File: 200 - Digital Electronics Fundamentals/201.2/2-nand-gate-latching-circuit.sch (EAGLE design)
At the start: 5 parts, among them IC1 74ALS00N

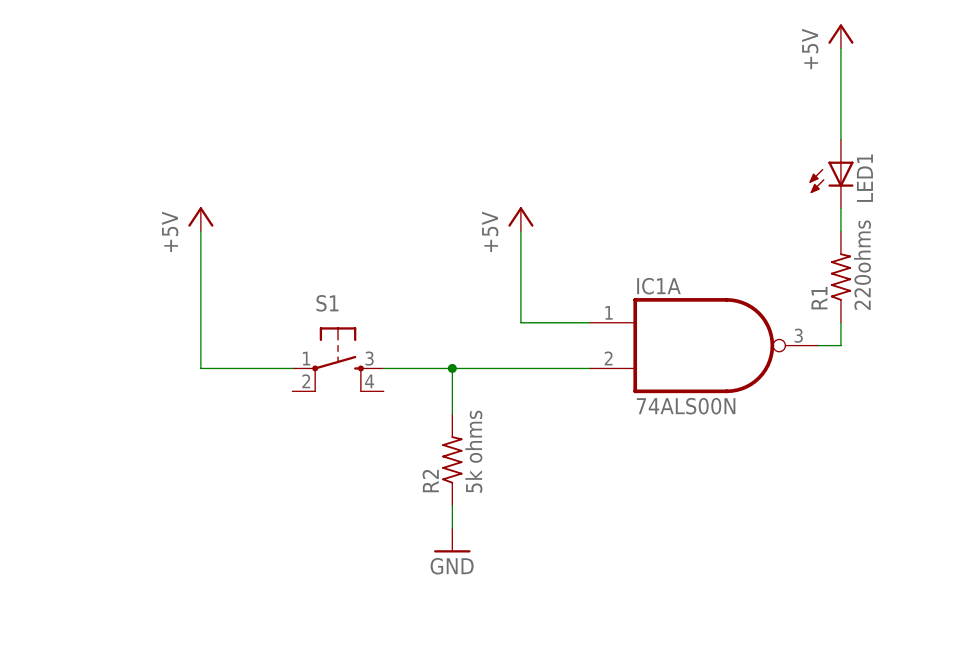
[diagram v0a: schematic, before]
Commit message: Made minor changes to Lab2 schematic.
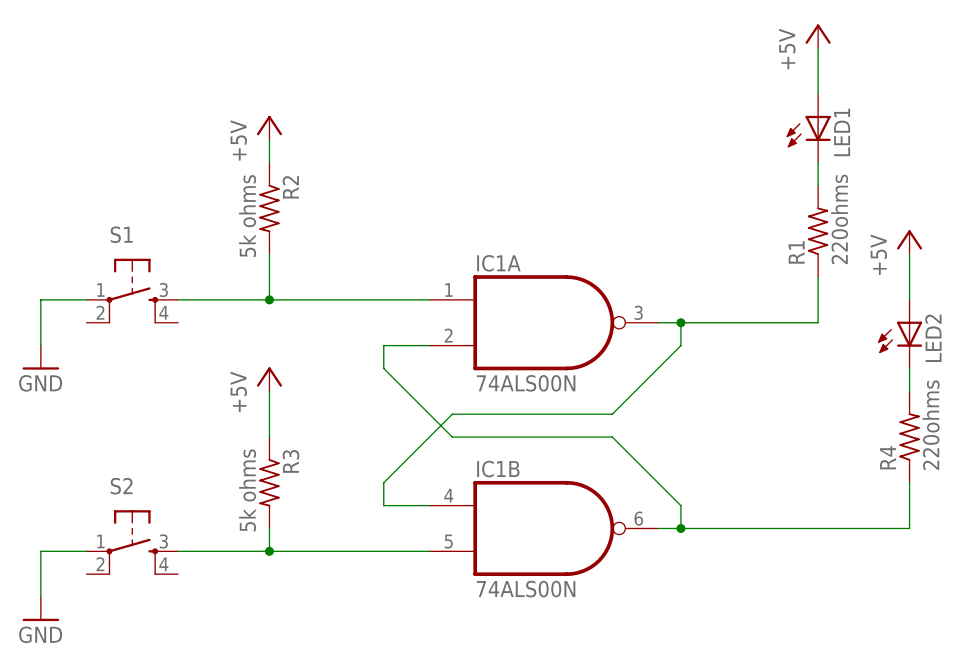
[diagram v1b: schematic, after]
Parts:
- added LED2: (no value), adafruit:LED5MM
- added R3: 5k ohms, resistor:R-US_0204/7
- added R4: 220ohms, resistor:R-US_0204/7
- added S2: (no value), SparkFun-Electromechanical:TAC_SWITCHPTH
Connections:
- new net N$5: IC1A.I0, R2.2, S1.3
- new net N$6: IC1B.I1, R3.2, S2.3
- new net N$7: LED2.C, R4.2
- net +5V: now also LED2.A, R2.1, R3.1; no longer IC1A.I0, S1.1
- net GND: now also S1.1, S2.1; no longer R2.1
- net N$1: now also IC1B.O, R4.1; no longer R2.2, S1.3
- net N$2: now also IC1B.I0
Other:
- moved on the sheet: IC1A, LED1, R1, R2, S1
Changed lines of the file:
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@@
 <part name="LED1" library="adafruit" deviceset="LED" device="5MM"/>
 <part name="R1" library="resistor" deviceset="R-US_" device="0204/7" value="220ohms"/>
-<part name="R2" library="resistor" deviceset="R-US_" device="0204/7" value="5k ohms"/>
 <part name="P+2" library="supply1" deviceset="+5V" device=""/>
 <part name="P+3" library="supply1" deviceset="+5V" device=""/>
+<part name="S2" library="SparkFun-Electromechanical" deviceset="TAC_SWITCH" device="PTH"/>
+<part name="R2" library="resistor" deviceset="R-US_" device="0204/7" value="5k ohms"/>
+<part name="R3" library="resistor" deviceset="R-US_" device="0204/7" value="5k ohms"/>
+<part name="GND2" library="supply1" deviceset="GND" device=""/>
+<part name="LED2" library="adafruit" deviceset="LED" device="5MM"/>
+<part name="R4" library="resistor" deviceset="R-US_" device="0204/7" value="220ohms"/>
+<part name="P+4" library="supply1" deviceset="+5V" device=""/>
 </parts>
 <sheets>
@@
 <instances>
 <instance part="U$1" gate="G$1" x="0" y="0"/>
-<instance part="IC1" gate="A" x="152.4" y="83.82"/>
-<instance part="S1" gate="S" x="111.76" y="81.28"/>
-<instance part="P+1" gate="1" x="132.08" y="99.06"/>
-<instance part="GND1" gate="1" x="124.46" y="60.96"/>
-<instance part="LED1" gate="G$1" x="167.64" y="104.14"/>
-<instance part="R1" gate="G$1" x="167.64" y="91.44" rot="R90"/>
-<instance part="R2" gate="G$1" x="124.46" y="71.12" rot="R90"/>
-<instance part="P+2" gate="1" x="96.52" y="99.06"/>
-<instance part="P+3" gate="1" x="167.64" y="119.38"/>
+<instance part="IC1" gate="A" x="134.62" y="86.36"/>
+<instance part="S1" gate="S" x="88.9" y="88.9"/>
+<instance part="P+1" gate="1" x="104.14" y="109.22"/>
+<instance part="GND1" gate="1" x="78.74" y="53.34"/>
+<instance part="LED1" gate="G$1" x="165.1" y="109.22"/>
+<instance part="R1" gate="G$1" x="165.1" y="96.52" rot="R90"/>
+<instance part="P+2" gate="1" x="104.14" y="81.28"/>
+<instance part="P+3" gate="1" x="165.1" y="119.38"/>
+<instance part="S2" gate="S" x="88.9" y="60.96"/>
+<instance part="IC1" gate="B" x="134.62" y="63.5"/>
+<instance part="R2" gate="G$1" x="104.14" y="99.06" rot="R270"/>
+<instance part="R3" gate="G$1" x="104.14" y="68.58" rot="R270"/>
+<instance part="GND2" gate="1" x="78.74" y="81.28"/>
+<instance part="LED2" gate="G$1" x="175.26" y="86.36"/>
+<instance part="R4" gate="G$1" x="175.26" y="73.66" rot="R90"/>
+<instance part="P+4" gate="1" x="175.26" y="96.52"/>
 </instances>
 <busses>
@@
 <net name="+5V" class="0">
 <segment>
-<pinref part="IC1" gate="A" pin="I0"/>
-<pinref part="P+1" gate="1" pin="+5V"/>
-<wire x1="139.7" y1="86.36" x2="132.08" y2="86.36" width="0.1524" layer="91"/>
-<wire x1="132.08" y1="86.36" x2="132.08" y2="96.52" width="0.1524" layer="91"/>
+<pinref part="P+3" gate="1" pin="+5V"/>
+<pinref part="LED1" gate="G$1" pin="A"/>
+<wire x1="165.1" y1="116.84" x2="165.1" y2="111.76" width="0.1524" layer="91"/>
 </segment>
 <segment>
-<pinref part="S1" gate="S" pin="1"/>
-<pinref part="P+2" gate="1" pin="+5V"/>
-<wire x1="106.68" y1="81.28" x2="96.52" y2="81.28" width="0.1524" layer="91"/>
-<wire x1="96.52" y1="81.28" x2="96.52" y2="96.52" width="0.1524" layer="91"/>
+<pinref part="R2" gate="G$1" pin="1"/>
+<pinref part="P+1" gate="1" pin="+5V"/>
+<wire x1="104.14" y1="104.14" x2="104.14" y2="106.68" width="0.1524" layer="91"/>
 </segment>
 <segment>
-<pinref part="P+3" gate="1" pin="+5V"/>
-<pinref part="LED1" gate="G$1" pin="A"/>
-<wire x1="167.64" y1="116.84" x2="167.64" y2="106.68" width="0.1524" layer="91"/>
+<pinref part="P+2" gate="1" pin="+5V"/>
+<pinref part="R3" gate="G$1" pin="1"/>
+<wire x1="104.14" y1="78.74" x2="104.14" y2="73.66" width="0.1524" layer="91"/>
 </segment>
-</net>
-<net name="N$1" class="0">
 <segment>
-<pinref part="IC1" gate="A" pin="I1"/>
-<pinref part="R2" gate="G$1" pin="2"/>
-<wire x1="139.7" y1="81.28" x2="124.46" y2="81.28" width="0.1524" layer="91"/>
-<wire x1="124.46" y1="81.28" x2="124.46" y2="76.2" width="0.1524" layer="91"/>
-<pinref part="S1" gate="S" pin="3"/>
-<wire x1="116.84" y1="81.28" x2="124.46" y2="81.28" width="0.1524" layer="91"/>
-<junction x="124.46" y="81.28"/>
-</segment>
-</net>
-<net name="GND" class="0">
-<segment>
-<pinref part="R2" gate="G$1" pin="1"/>
-<pinref part="GND1" gate="1" pin="GND"/>
-<wire x1="124.46" y1="66.04" x2="124.46" y2="63.5" width="0.1524" layer="91"/>
-</segment>
-</net>
-<net name="N$2" class="0">
-<segment>
-<pinref part="IC1" gate="A" pin="O"/>
-<pinref part="R1" gate="G$1" pin="1"/>
-<wire x1="165.1" y1="83.82" x2="167.64" y2="83.82" width="0.1524" layer="91"/>
-<wire x1="167.64" y1="83.82" x2="167.64" y2="86.36" width="0.1524" layer="91"/>
+<pinref part="P+4" gate="1" pin="+5V"/>
+<pinref part="LED2" gate="G$1" pin="A"/>
+<wire x1="175.26" y1="93.98" x2="175.26" y2="88.9" width="0.1524" layer="91"/>
 </segment>
 </net>
@@
 <pinref part="LED1" gate="G$1" pin="C"/>
 <pinref part="R1" gate="G$1" pin="2"/>
-<wire x1="167.64" y1="99.06" x2="167.64" y2="96.52" width="0.1524" layer="91"/>
+<wire x1="165.1" y1="104.14" x2="165.1" y2="101.6" width="0.1524" layer="91"/>
 </segment>
 </net>
+<net name="N$1" class="0">
+<segment>
+<pinref part="IC1" gate="B" pin="O"/>
+<wire x1="147.32" y1="63.5" x2="149.86" y2="63.5" width="0.1524" layer="91"/>
+<wire x1="149.86" y1="63.5" x2="175.26" y2="63.5" width="0.1524" layer="91"/>
+<wire x1="149.86" y1="63.5" x2="149.86" y2="66.04" width="0.1524" layer="91"/>
+<wire x1="149.86" y1="66.04" x2="142.24" y2="73.66" width="0.1524" layer="91"/>
+<wire x1="142.24" y1="73.66" x2="124.46" y2="73.66" width="0.1524" layer="91"/>
+<wire x1="124.46" y1="73.66" x2="116.84" y2="81.28" width="0.1524" layer="91"/>
+<pinref part="IC1" gate="A" pin="I1"/>
+<wire x1="116.84" y1="81.28" x2="116.84" y2="83.82" width="0.1524" layer="91"/>
+<wire x1="116.84" y1="83.82" x2="121.92" y2="83.82" width="0.1524" layer="91"/>
+<junction x="149.86" y="63.5"/>
+<pinref part="R4" gate="G$1" pin="1"/>
+<wire x1="175.26" y1="63.5" x2="175.26" y2="68.58" width="0.1524" layer="91"/>
+</segment>
+</net>
+<net name="N$2" class="0">
+<segment>
+<pinref part="IC1" gate="A" pin="O"/>
+<wire x1="147.32" y1="86.36" x2="149.86" y2="86.36" width="0.1524" layer="91"/>
+<pinref part="IC1" gate="B" pin="I0"/>
+<wire x1="149.86" y1="86.36" x2="165.1" y2="86.36" width="0.1524" layer="91"/>
+<wire x1="121.92" y1="66.04" x2="116.84" y2="66.04" width="0.1524" layer="91"/>
+<wire x1="116.84" y1="66.04" x2="116.84" y2="68.58" width="0.1524" layer="91"/>
+<wire x1="116.84" y1="68.58" x2="124.46" y2="76.2" width="0.1524" layer="91"/>
+<wire x1="124.46" y1="76.2" x2="142.24" y2="76.2" width="0.1524" layer="91"/>
+<wire x1="142.24" y1="76.2" x2="149.86" y2="83.82" width="0.1524" layer="91"/>
+<wire x1="149.86" y1="83.82" x2="149.86" y2="86.36" width="0.1524" layer="91"/>
+<junction x="149.86" y="86.36"/>
+<pinref part="R1" gate="G$1" pin="1"/>
+<wire x1="165.1" y1="86.36" x2="165.1" y2="91.44" width="0.1524" layer="91"/>
+</segment>
+</net>
+<net name="N$5" class="0">
+<segment>
+<pinref part="IC1" gate="A" pin="I0"/>
+<pinref part="R2" gate="G$1" pin="2"/>
+<wire x1="121.92" y1="88.9" x2="104.14" y2="88.9" width="0.1524" layer="91"/>
+<wire x1="104.14" y1="88.9" x2="104.14" y2="93.98" width="0.1524" layer="91"/>
+<pinref part="S1" gate="S" pin="3"/>
+<wire x1="93.98" y1="88.9" x2="104.14" y2="88.9" width="0.1524" layer="91"/>
+<junction x="104.14" y="88.9"/>
+</segment>
+</net>
+<net name="N$6" class="0">
+<segment>
+<pinref part="IC1" gate="B" pin="I1"/>
+<pinref part="R3" gate="G$1" pin="2"/>
+<wire x1="121.92" y1="60.96" x2="104.14" y2="60.96" width="0.1524" layer="91"/>
+<wire x1="104.14" y1="60.96" x2="104.14" y2="63.5" width="0.1524" layer="91"/>
+<pinref part="S2" gate="S" pin="3"/>
+<wire x1="93.98" y1="60.96" x2="104.14" y2="60.96" width="0.1524" layer="91"/>
+<junction x="104.14" y="60.96"/>
+</segment>
+</net>
+<net name="GND" class="0">
+<segment>
+<pinref part="S1" gate="S" pin="1"/>
+<pinref part="GND2" gate="1" pin="GND"/>
+<wire x1="83.82" y1="88.9" x2="78.74" y2="88.9" width="0.1524" layer="91"/>
+<wire x1="78.74" y1="88.9" x2="78.74" y2="83.82" width="0.1524" layer="91"/>
+</segment>
+<segment>
+<pinref part="S2" gate="S" pin="1"/>
+<pinref part="GND1" gate="1" pin="GND"/>
+<wire x1="83.82" y1="60.96" x2="78.74" y2="60.96" width="0.1524" layer="91"/>
+<wire x1="78.74" y1="60.96" x2="78.74" y2="55.88" width="0.1524" layer="91"/>
+</segment>
+</net>
+<net name="N$7" class="0">
+<segment>
+<pinref part="LED2" gate="G$1" pin="C"/>
+<pinref part="R4" gate="G$1" pin="2"/>
+<wire x1="175.26" y1="81.28" x2="175.26" y2="78.74" width="0.1524" layer="91"/>
+</segment>
+</net>
